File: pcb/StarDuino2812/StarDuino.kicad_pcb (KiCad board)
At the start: 2 copper layers, 114.2 x 108.6 mm, 86 parts, among them J1 Screw_Terminal_01x02, J2 Conn_01x03_Male, J3 Conn_01x01_Male, Q1 IRLML6401, U1 ATmega328P-AU, Y1 16M

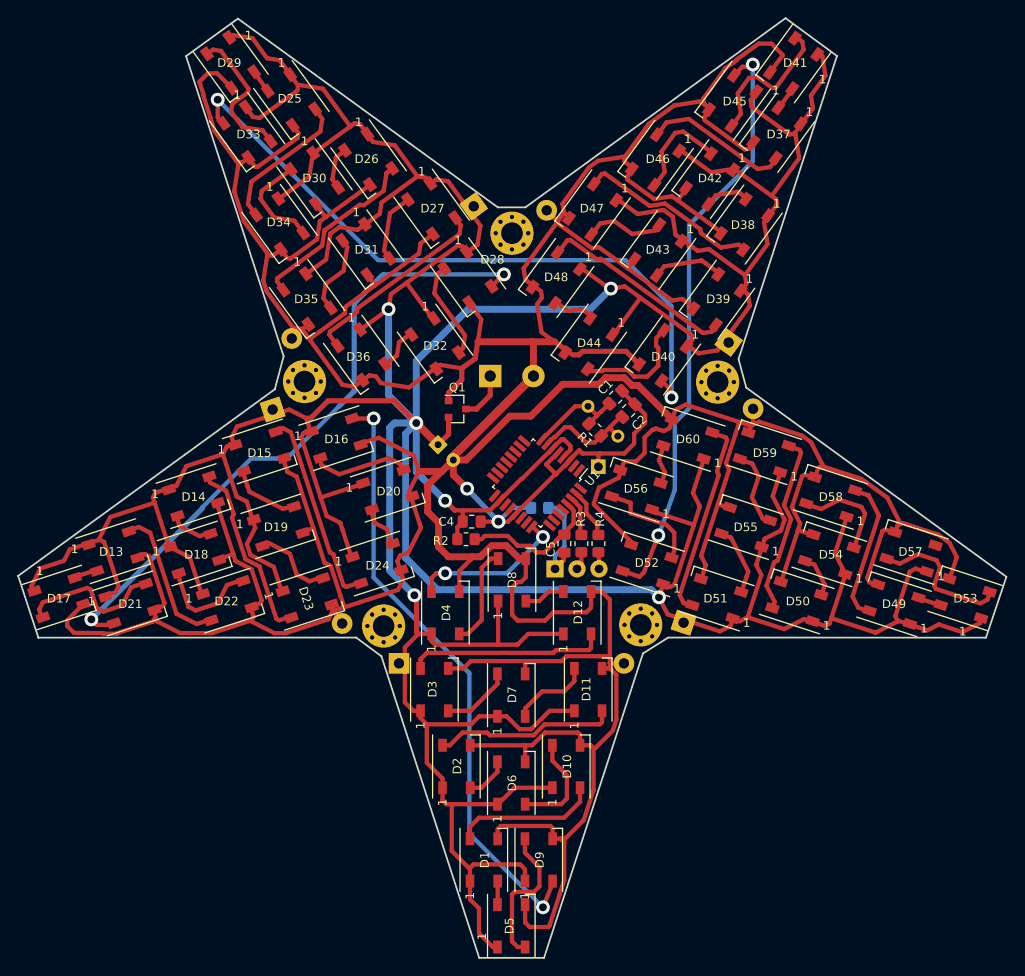
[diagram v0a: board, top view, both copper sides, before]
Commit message: NewYearStar2812. Add capacitors.
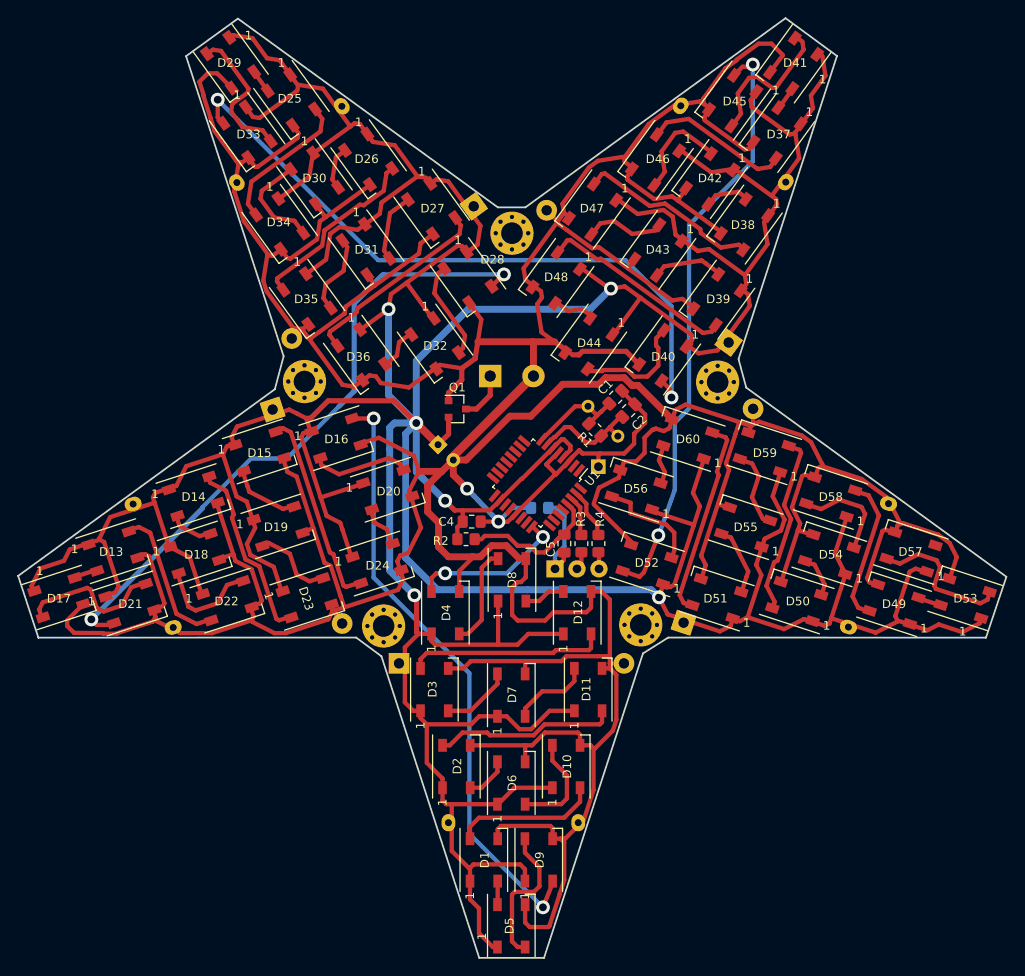
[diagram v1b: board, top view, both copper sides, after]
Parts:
- added C11: 0.1uF, Capacitor_THT:C_Rect_L19.0mm_W5.0mm_P15.00mm_MKS4, B.Cu at (61.0, 97.0)
- added C12: 0.1uF, Capacitor_THT:C_Rect_L19.0mm_W5.0mm_P15.00mm_MKS4, B.Cu at (136.4, 59.8)
- added C13: 0.1uF, Capacitor_THT:C_Rect_L19.0mm_W5.0mm_P15.00mm_MKS4, B.Cu at (85.1, 51.1)
- added C14: 0.1uF, Capacitor_THT:C_Rect_L19.0mm_W5.0mm_P15.00mm_MKS4, B.Cu at (97.4, 133.9)
- added C15: 0.1uF, Capacitor_THT:C_Rect_L19.0mm_W5.0mm_P15.00mm_MKS4, B.Cu at (143.6, 111.3)
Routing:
- net VCC: track 711.0 -> 713.5 mm

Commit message: StarDuino2812. Fix hash. Add photomask
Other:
- board text added: "174b82"
- board text added: "22.09.2021"
- board text added: "StarDuino"

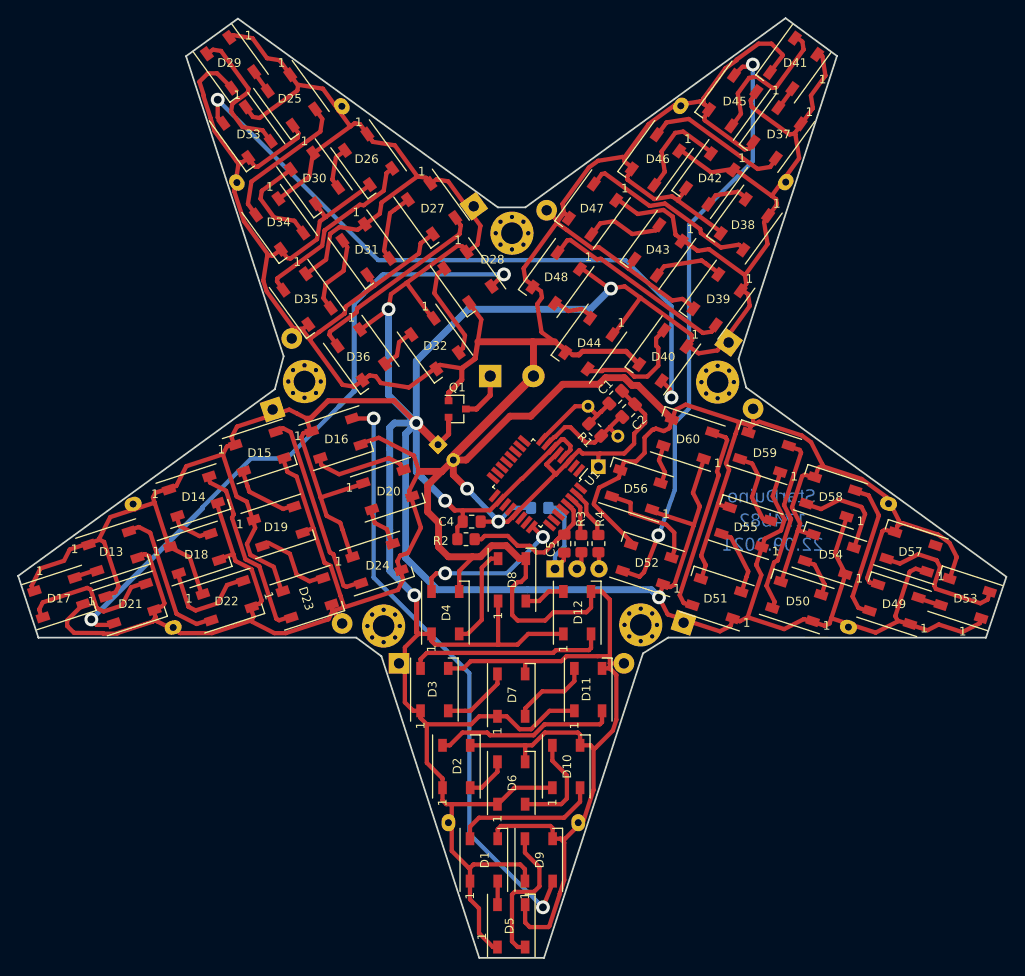
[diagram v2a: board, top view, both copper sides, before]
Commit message: Replace disk capacitor. Add gerber.
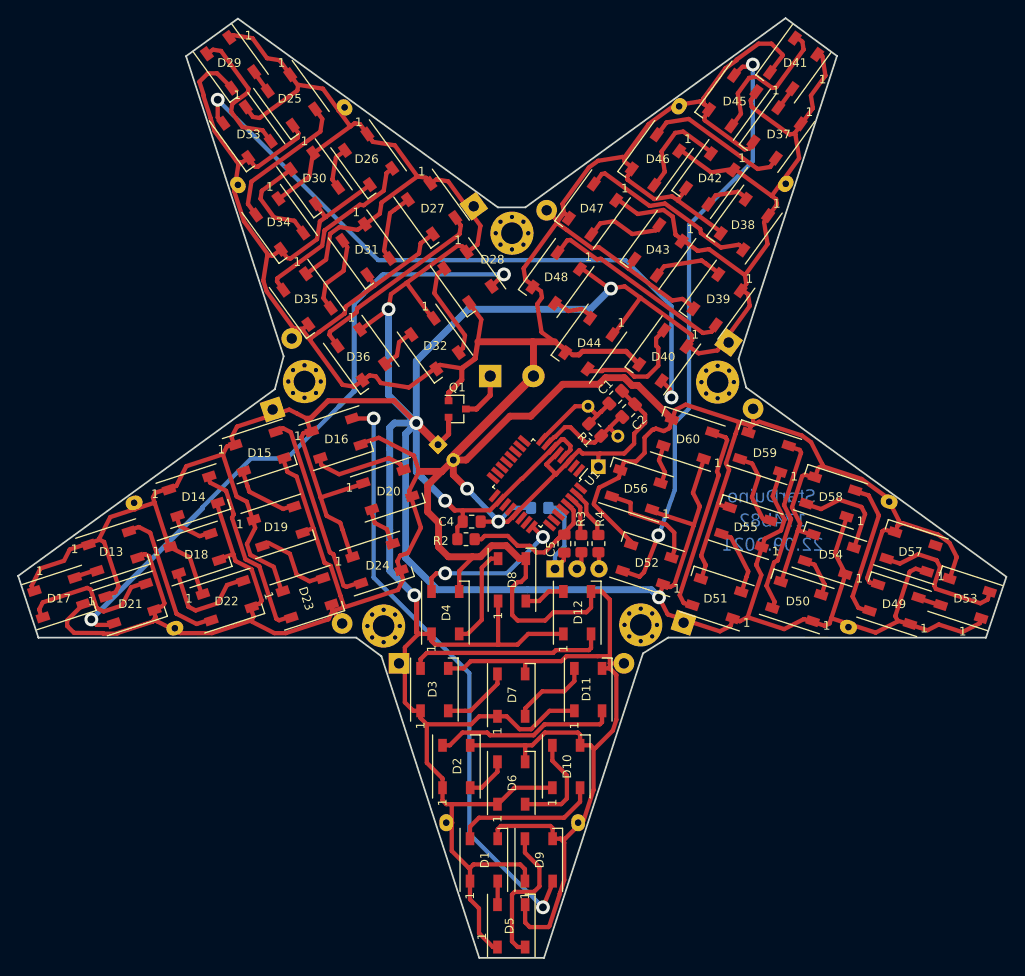
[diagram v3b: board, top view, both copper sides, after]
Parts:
- C11, C12, C13, C14, C15: footprint Capacitor_THT:C_Rect_L19.0mm_W5.0mm_P15.00mm_MKS4 -> CommonLibrary:C-disk-15mm
- moved C13 0.34 mm to (85.4, 51.2)
- moved C14 0.25 mm to (97.2, 133.9)
- moved C12 0.19 mm to (136.4, 60.0)
- moved C11 0.18 mm to (61.1, 96.9)

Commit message: Add ISP to StarDuino
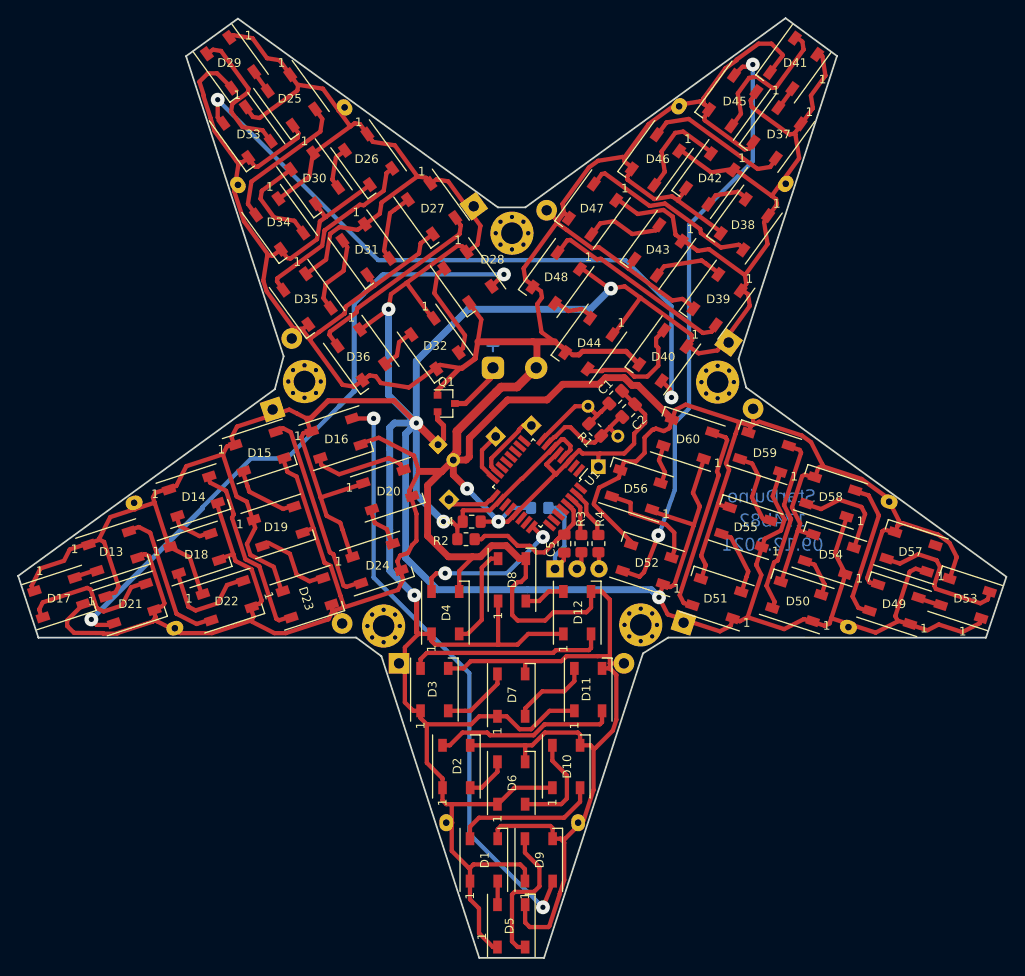
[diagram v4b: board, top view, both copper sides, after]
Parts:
- added J4: Conn_01x01_Male, Connector_PinHeader_2.54mm:PinHeader_1x01_P2.54mm_Vertical, B.Cu at (107.0, 87.9)
- added J5: Conn_01x01_Male, Connector_PinHeader_2.54mm:PinHeader_1x01_P2.54mm_Vertical, B.Cu at (102.9, 89.2)
- added J6: Conn_01x01_Male, Connector_PinHeader_2.54mm:PinHeader_1x01_P2.54mm_Vertical, B.Cu at (97.5, 96.5)
- moved Q1 1.42 mm to (97.2, 85.4)
- moved J1 1.00 mm to (102.6, 81.3)
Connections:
- U1 pad 15: Net-(U1-Pad15) -> /MOSI
- U1 pad 16: Net-(U1-Pad16) -> /MISO
- U1 pad 17: Net-(U1-Pad17) -> /SCK
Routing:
- net /MOSI: track 0.00 -> 8.24 mm
- net /MISO: track 0.00 -> 6.00 mm
- net /SCK: track 0.00 -> 5.91 mm
- net GND: track 741.9 -> 744.9 mm
- net (no net): track 0.00 -> 2.54 mm
- net VCC: track 713.5 -> 715.9 mm
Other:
- board text added: "09.12.2021"
- board text added: "MISO"
- board text added: "MOSI"
- board text added: "SCK"
- board text removed: "22.09.2021"
